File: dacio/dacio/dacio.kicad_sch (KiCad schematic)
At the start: 56 parts, among them J3 RJ45_Shielded, J4 RJ45_Shielded, J5 Conn_02x12_Odd_Even, U1 SN74LVC1T45DBV, U10 MAX3232, U11 MAX3232, U12 74HCT32D, U13 74HCT00D, U14 74HCT32D, U15 74HCT00D, U16 TLV70033_SOT353, U17 SN74LV8T374PWR, U18 SN74LV8T374PWR, U2 SN74LVC1T45DBV, U3 TLV70018_SOT353, U4 MAX487CSA+, U5 MAX487CSA+, U6 MAX487CSA+, U7 MAX487CSA+, U8 MAX487CSA+, U9 MAX487CSA+

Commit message: Use the correct pin-headers.
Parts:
- J1, J2: footprint Connector_PinHeader_2.54mm:PinHeader_2x12_P2.54mm_Vertical -> Connector_PinSocket_2.54mm:PinSocket_2x12_P2.54mm_Vertical
- J5: footprint Connector_PinSocket_2.54mm:PinSocket_2x12_P2.54mm_Vertical -> Connector_PinHeader_2.54mm:PinHeader_2x12_P2.54mm_Vertical
- U17, U18: footprint TSSOP-20_4.4x6.5mm_P0.65mm -> Package_SO:Texas_PW0020A_TSSOP-20_4.4x6.5mm_P0.65mm
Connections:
- net 5v: now also J2.17 (5v), J2.19 (5v)
- net GND: now also J1.11 (GND), J1.14 (GND), J1.17 (GND), J1.2 (GND), J1.20 (GND), J1.23 (GND), J1.5 (GND), J1.8 (GND), J2.10 (GND), J2.13 (GND), J2.15 (GND), J2.16 (GND), J2.18 (GND), J2.2 (GND), J2.20 (GND), J2.21 (GND), J2.23 (GND), J2.5 (GND), J2.7 (GND), J2.8 (GND)
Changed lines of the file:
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@@
 	(wire
 		(pts
+			(xy 41.91 163.83) (xy 41.91 165.1)
+		)
+		(stroke
+			(width 0)
+			(type default)
+		)
+	)
+	(wire
+		(pts
 			(xy 241.3 262.89) (xy 241.3 260.35)
 		)
@@
 	(wire
 		(pts
+			(xy 19.05 175.26) (xy 21.59 175.26)
+		)
+		(stroke
+			(width 0)
+			(type default)
+		)
+	)
+	(wire
+		(pts
 			(xy 31.75 238.76) (xy 35.56 238.76)
 		)
@@
 	(wire
 		(pts
+			(xy 19.05 179.07) (xy 21.59 179.07)
+		)
+		(stroke
+			(width 0)
+			(type default)
+		)
+	)
+	(wire
+		(pts
 			(xy 358.14 162.56) (xy 358.14 170.18)
 		)
@@
 		)
 	)
+	(global_label "GND"
+		(shape passive)
+		(at 19.05 179.07 180)
+		(fields_autoplaced yes)
+		(effects
+			(font
+				(size 1.27 1.27)
+			)
+			(justify right)
+		)
+		(property "Intersheetrefs" "${INTERSHEET_REFS}"
+			(at 13.3056 179.07 0)
+			(hide yes)
+			(show_name no)
+			(do_not_autoplace no)
+			(effects
+				(font
+					(size 1.27 1.27)
+				)
+				(justify right)
+			)
+		)
+	)
 	(global_label "HDR_RF_SEL2"
 		(shape output)
@@
 		)
 	)
+	(global_label "GND"
+		(shape passive)
+		(at 41.91 165.1 270)
+		(fields_autoplaced yes)
+		(effects
+			(font
+				(size 1.27 1.27)
+			)
+			(justify right)
+		)
+		(property "Intersheetrefs" "${INTERSHEET_REFS}"
+			(at 41.91 170.8444 90)
+			(hide yes)
+			(show_name no)
+			(do_not_autoplace no)
+			(effects
+				(font
+					(size 1.27 1.27)
+				)
+				(justify right)
+			)
+		)
+	)
 	(global_label "HDR_RF_SEL0"
 		(shape input)
@@
 		)
 	)
+	(global_label "5v"
+		(shape passive)
+		(at 19.05 175.26 180)
+		(fields_autoplaced yes)
+		(effects
+			(font
+				(size 1.27 1.27)
+			)
+			(justify right)
+		)
+		(property "Intersheetrefs" "${INTERSHEET_REFS}"
+			(at 14.999 175.26 0)
+			(hide yes)
+			(show_name no)
+			(do_not_autoplace no)
+			(effects
+				(font
+					(size 1.27 1.27)
+				)
+				(justify right)
+			)
+		)
+	)
 	(global_label "HDR_LEV0"
 		(shape input)
@@
 			)
 		)
-		(property "Footprint" "TSSOP-20_4.4x6.5mm_P0.65mm"
+		(property "Footprint" "Package_SO:Texas_PW0020A_TSSOP-20_4.4x6.5mm_P0.65mm"
 			(at 132.08 251.46 0)
 			(hide yes)
@@
 			)
 		)
-		(property "Footprint" "Connector_PinSocket_2.54mm:PinSocket_2x12_P2.54mm_Vertical"
+		(property "Footprint" "Connector_PinHeader_2.54mm:PinHeader_2x12_P2.54mm_Vertical"
 			(at 68.58 201.93 0)
 			(hide yes)
@@
 			)
 		)
-		(property "Footprint" "Connector_PinHeader_2.54mm:PinHeader_2x12_P2.54mm_Vertical"
+		(property "Footprint" "Connector_PinSocket_2.54mm:PinSocket_2x12_P2.54mm_Vertical"
 			(at 30.48 149.86 0)
 			(hide yes)
@@
 			)
 		)
-		(property "Footprint" "Connector_PinHeader_2.54mm:PinHeader_2x12_P2.54mm_Vertical"
+		(property "Footprint" "Connector_PinSocket_2.54mm:PinSocket_2x12_P2.54mm_Vertical"
 			(at 21.59 176.53 0)
 			(hide yes)
@@
 			)
 		)
-		(property "Footprint" "TSSOP-20_4.4x6.5mm_P0.65mm"
+		(property "Footprint" "Package_SO:Texas_PW0020A_TSSOP-20_4.4x6.5mm_P0.65mm"
 			(at 48.26 251.46 0)
 			(hide yes)

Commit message: Fixed some of the layout.
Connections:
- net GND: now also J5.14 (Pin_14), J5.15 (Pin_15), J5.19 (Pin_19), J5.5 (Pin_5); no longer J5.10 (Pin_10), J5.17 (Pin_17), J5.18 (Pin_18), J5.22 (Pin_22)
- net HIGH_DIR0: now also J5.20 (Pin_20); no longer J5.12 (Pin_12)
- net HIGH_DIR1: now also J5.17 (Pin_17); no longer J5.14 (Pin_14)
- net HIGH_DIR2: now also J5.18 (Pin_18); no longer J5.16 (Pin_16)
- net HIGH_ERR: now also J5.16 (Pin_16); no longer J5.20 (Pin_20)
- net HIGH_LEV0: now also J5.23 (Pin_23); no longer J5.2 (Pin_2)
- net HIGH_LEV1: now also J5.24 (Pin_24); no longer J5.4 (Pin_4)
- net HIGH_LEV2: now also J5.21 (Pin_21); no longer J5.6 (Pin_6)
- net HIGH_LEV3: now also J5.22 (Pin_22); no longer J5.8 (Pin_8)
- net LED_CLK: now also J5.11 (Pin_11); no longer J5.21 (Pin_21)
- net LED_CS: no longer J5.24 (Pin_24)
- net LED_OUT: now also J5.12 (Pin_12); no longer J5.23 (Pin_23)
- net LOW_DIR0: now also J5.6 (Pin_6); no longer J5.11 (Pin_11)
- net LOW_DIR1: now also J5.7 (Pin_7); no longer J5.13 (Pin_13)
- net LOW_DIR2: now also J5.8 (Pin_8); no longer J5.15 (Pin_15)
- net LOW_ERR: now also J5.10 (Pin_10); no longer J5.19 (Pin_19)
- net LOW_LEV1: now also J5.2 (Pin_2); no longer J5.3 (Pin_3)
- net LOW_LEV2: now also J5.3 (Pin_3); no longer J5.5 (Pin_5)
- net LOW_LEV3: now also J5.4 (Pin_4); no longer J5.7 (Pin_7)

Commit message: Finalized layout for DACIO.
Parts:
- removed C14, C2, C21, C23: 100n, Capacitor_SMD:C_0805_2012Metric_Pad1.18x1.45mm_HandSolder, symbol Device:C
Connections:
- net LED_CS: now also J5.13 (Pin_13)
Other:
- moved on the sheet: C22, C24, C25, C27

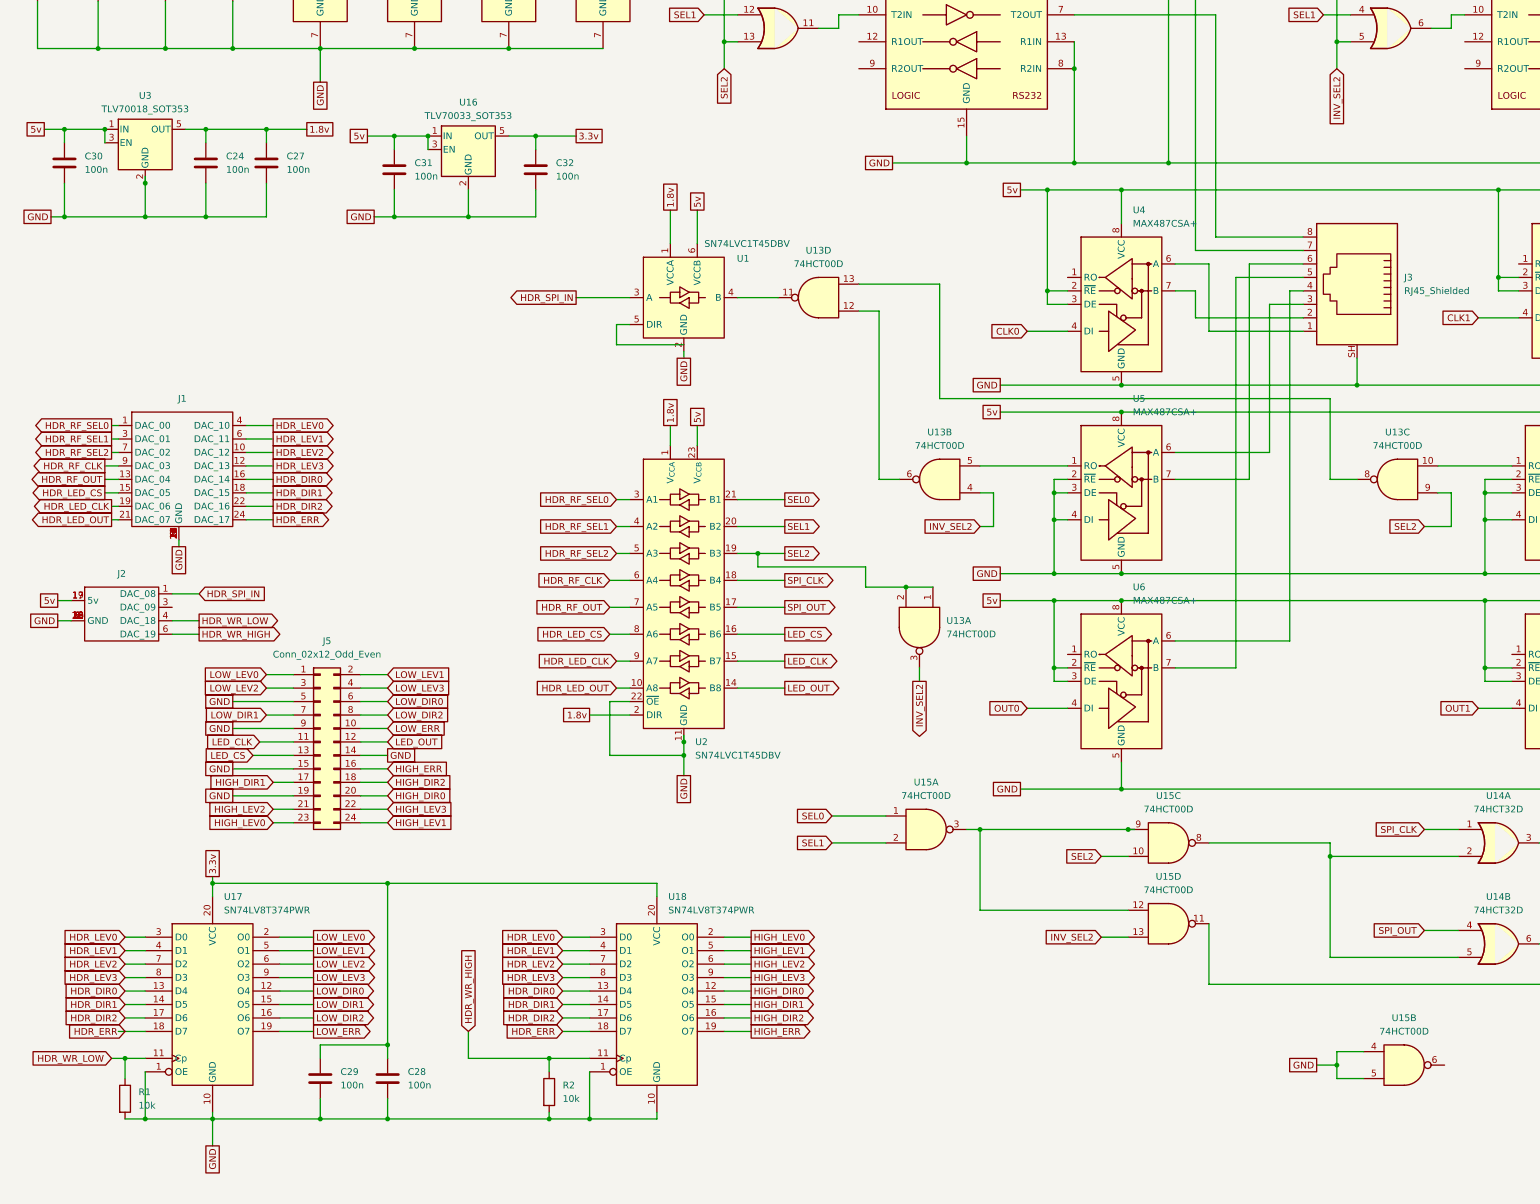
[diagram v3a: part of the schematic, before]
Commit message: Changed debug-header to data & address bus
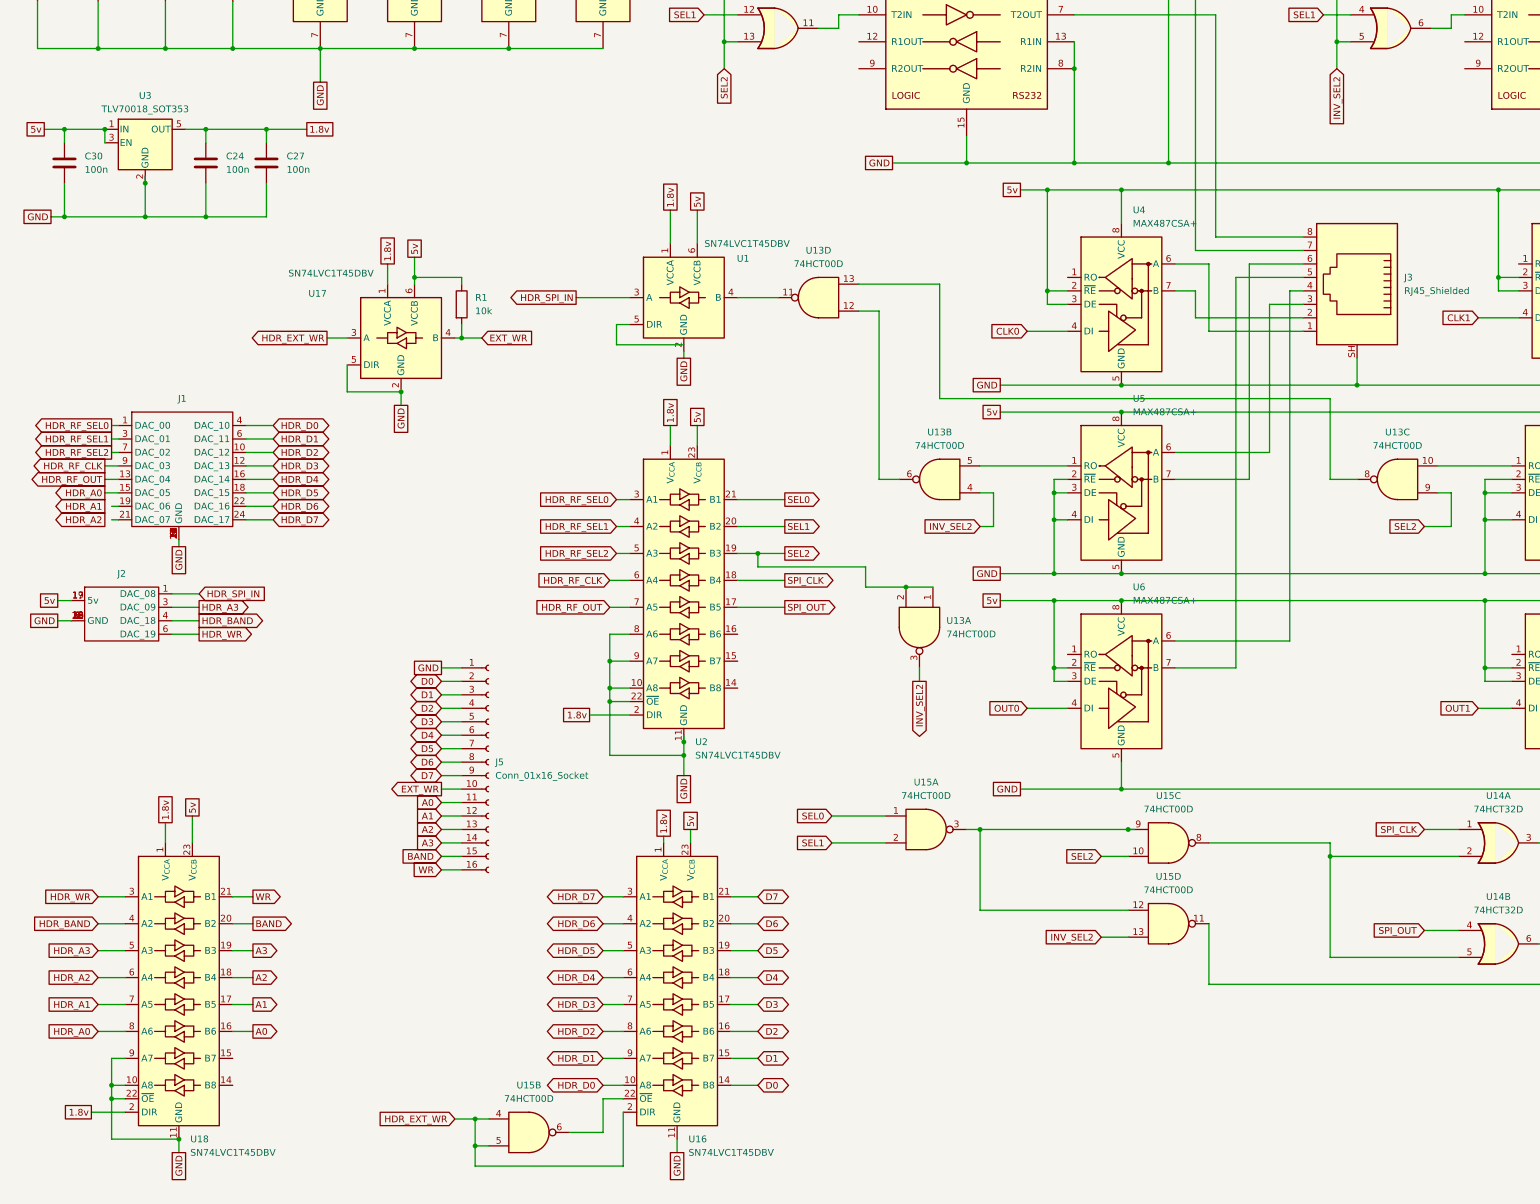
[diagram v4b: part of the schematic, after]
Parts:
- removed C28, C29, C31, C32: 100n, Capacitor_SMD:C_0805_2012Metric_Pad1.18x1.45mm_HandSolder, symbol Device:C
- removed J5: Conn_02x12_Odd_Even, Connector_PinHeader_2.54mm:PinHeader_2x12_P2.54mm_Vertical, symbol Connector_Generic:Conn_02x12_Odd_Even
- removed R2: 10k, Resistor_SMD:R_0805_2012Metric_Pad1.20x1.40mm_HandSolder, symbol Device:R
- removed U16: TLV70033_SOT353, Package_TO_SOT_SMD:SOT-353_SC-70-5, symbol Regulator_Linear:TLV70018_SOT353
- removed U17, U18: SN74LV8T374PWR, Package_SO:Texas_PW0020A_TSSOP-20_4.4x6.5mm_P0.65mm, symbol 74xx:74LS374
- added J5: Conn_01x16_Socket, Connector_PinHeader_2.54mm:PinHeader_1x16_P2.54mm_Vertical, symbol Connector:Conn_01x16_Socket
- added U16, U18: SN74LVC1T45DBV, Package_SO:TSSOP-24_4.4x7.8mm_P0.65mm, symbol Logic_LevelTranslator:SN74LVC8T245
- added U17: SN74LVC1T45DBV, Package_TO_SOT_SMD:SOT-23-6, symbol Logic_LevelTranslator:SN74LVC1T45DBV
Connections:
- net 1.8v: now also U16.1 (V_{CCA}), U17.1 (VCCA), U18.1 (V_{CCA}), U18.2 (DIR)
- net 5v: now also R1.1, U16.23 (V_{CCB}), U16.24 (V_{CCB}), U17.6 (VCCB), U18.23 (V_{CCB}), U18.24 (V_{CCB})
- net GND: now also U2.10 (A8), U2.8 (A6), U2.9 (A7), J5.1 (Pin_1), U16.11 (GND), U16.12 (GND), U16.13 (GND), U17.2 (GND), U17.5 (DIR), U18.10 (A8), U18.11 (GND), U18.12 (GND), U18.13 (GND), U18.22 (~{OE}), U18.9 (A7); no longer R1.2, U15.4, U15.5
- net at U15.6: now also U16.22 (~{OE})
- net HDR_A3: now reaches J2.3 (DAC_09)
- net HDR_A3: now also U18.5 (A3)
- net HDR_DIR0 renamed HDR_D4
- net HDR_D4: now also U16.6 (A4)
- net HDR_DIR1 renamed HDR_D5
- net HDR_D5: now also U16.5 (A3)
- net HDR_DIR2 renamed HDR_D6
- net HDR_D6: now also U16.4 (A2)
- net HDR_ERR renamed HDR_D7
- net HDR_D7: now also U16.3 (A1)
- net HDR_LED_CLK: no longer names the net of J1.19 (DAC_06)
- net HDR_LED_CLK: no longer U2.9 (A7)
- net HDR_LED_CS renamed HDR_A0
- net HDR_A0: now also U18.8 (A6); no longer U2.8 (A6)
- net HDR_LED_OUT: no longer names the net of J1.21 (DAC_07)
- net HDR_LED_OUT: no longer U2.10 (A8)
- net HDR_LEV0 renamed HDR_D0
- net HDR_D0: now also U16.10 (A8)
- net HDR_LEV1 renamed HDR_D1
- net HDR_D1: now also U16.9 (A7)
- net HDR_LEV2 renamed HDR_D2
- net HDR_D2: now also U16.8 (A6)
- net HDR_LEV3 renamed HDR_D3
- net HDR_D3: now also U16.7 (A5)
- net HDR_WR_HIGH renamed HDR_WR
- net HDR_WR: now also U18.3 (A1)
- net HDR_WR_LOW renamed HDR_BAND
- net HDR_BAND: now also U18.4 (A2); no longer R1.1
- net LED_CLK: no longer names the net of U2.15 (B7)
- net LED_CS: no longer names the net of U2.16 (B6)
- net LED_OUT: no longer names the net of U2.14 (B8)
- new net A0: J5.11 (Pin_11), U18.16 (B6)
- new net A1: J5.12 (Pin_12), U18.17 (B5)
- new net A2: J5.13 (Pin_13), U18.18 (B4)
- new net A3: J5.14 (Pin_14), U18.19 (B3)
- new net BAND: J5.15 (Pin_15), U18.20 (B2)
- new net D0: J5.2 (Pin_2), U16.14 (B8)
- new net D1: J5.3 (Pin_3), U16.15 (B7)
- new net D2: J5.4 (Pin_4), U16.16 (B6)
- new net D3: J5.5 (Pin_5), U16.17 (B5)
- new net D4: J5.6 (Pin_6), U16.18 (B4)
- new net D5: J5.7 (Pin_7), U16.19 (B3)
- new net D6: J5.8 (Pin_8), U16.20 (B2)
- new net D7: J5.9 (Pin_9), U16.21 (B1)
- new net EXT_WR: J5.10 (Pin_10), R1.2, U17.4 (B)
- new net HDR_A1: U18.7 (A5)
- new net HDR_A2: U18.6 (A4)
- new net HDR_EXT_WR: U15.4, U15.5, U16.2 (DIR), U17.3 (A)
- new net WR: J5.16 (Pin_16), U18.21 (B1)
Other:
- moved on the sheet: U15B

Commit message: fixed new layout
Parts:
- removed R1: 10k, Resistor_SMD:R_0805_2012Metric_Pad1.20x1.40mm_HandSolder, symbol Device:R
- removed U17: SN74LVC1T45DBV, Package_TO_SOT_SMD:SOT-23-6, symbol Logic_LevelTranslator:SN74LVC1T45DBV
- added C28, C29, C31, C32: 100n, Capacitor_SMD:C_0805_2012Metric_Pad1.18x1.45mm_HandSolder, symbol Device:C
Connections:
- net EXT_WR is gone; now on net GND: J5.10 (Pin_10)
- net 1.8v: now also U16.2 (DIR), C28.1, C29.1
- net 5v: now also C31.1, C32.1
- net GND: now also U15.4, U15.5, U16.22 (~{OE}), C28.2, C29.2, C31.2, C32.2
- net HDR_A1: now also J1.19 (DAC_06)
- net HDR_A2: now also J1.21 (DAC_07)
- net at U15.6: no longer U16.22 (~{OE})
- removed net HDR_EXT_WR: U15.4, U15.5, U16.2 (DIR)
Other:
- moved on the sheet: U15B

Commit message: Updated footprints for RJ45 and balun height.
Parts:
- J3, J4: footprint Connector_RJ:RJ45_Amphenol_RJHSE5380 -> custom:RJ45
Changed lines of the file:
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@@
 			)
 		)
-		(property "Footprint" "Connector_RJ:RJ45_Amphenol_RJHSE5380"
+		(property "Footprint" "custom:RJ45"
 			(at 347.98 117.475 90)
 			(hide yes)
@@
 			)
 		)
-		(property "Footprint" "Connector_RJ:RJ45_Amphenol_RJHSE5380"
+		(property "Footprint" "custom:RJ45"
 			(at 264.16 116.205 90)
 			(hide yes)
